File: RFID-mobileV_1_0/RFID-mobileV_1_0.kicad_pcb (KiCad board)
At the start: 2 copper layers, 52.9 x 145.1 mm, 53 parts, among them J1 USB_C_Receptacle_USB2.0, J2 Conn_01x05_Male, J3 Conn_01x05_Female, J4 Conn_01x05_Male, Q1 MMBT3904, SW1 SW_Push, U1 XC6206P332MR, U2 E22-400T22S, U3 STM32G030FxP, U4 LM321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

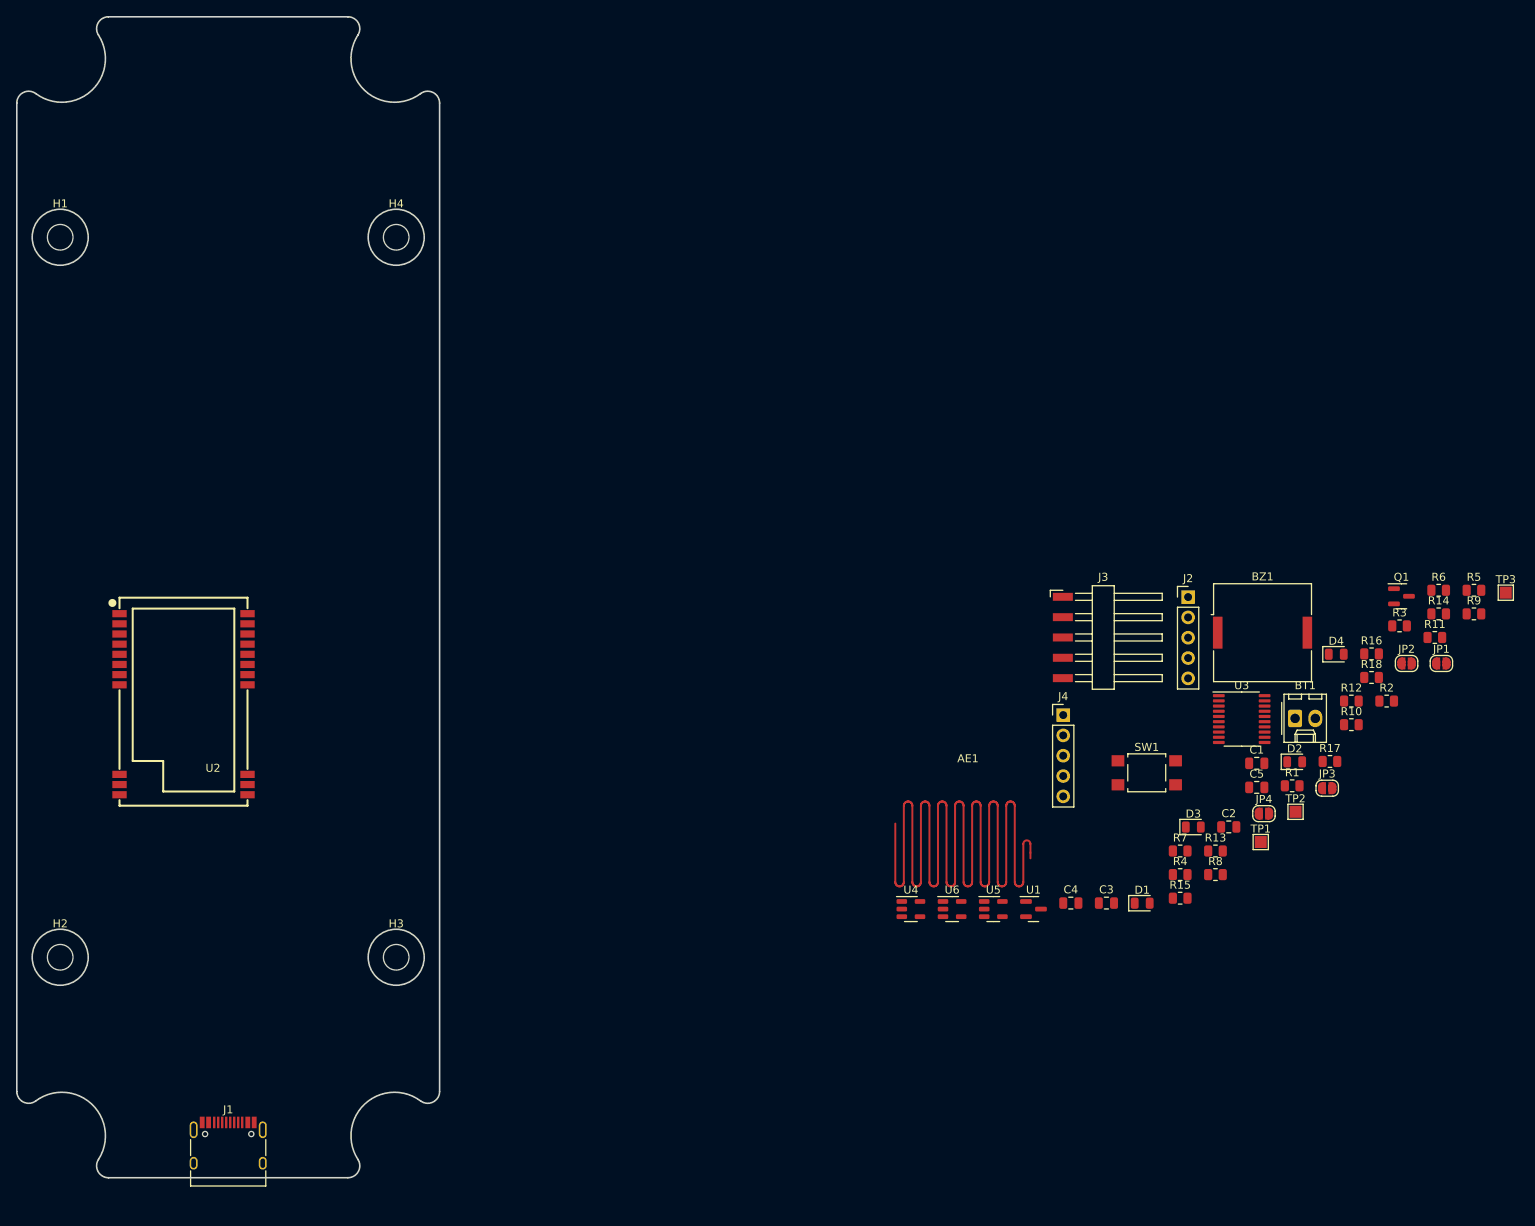
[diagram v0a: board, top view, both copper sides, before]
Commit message: Update RFID-mobileV_1_0.kicad_pcb
remove Case box
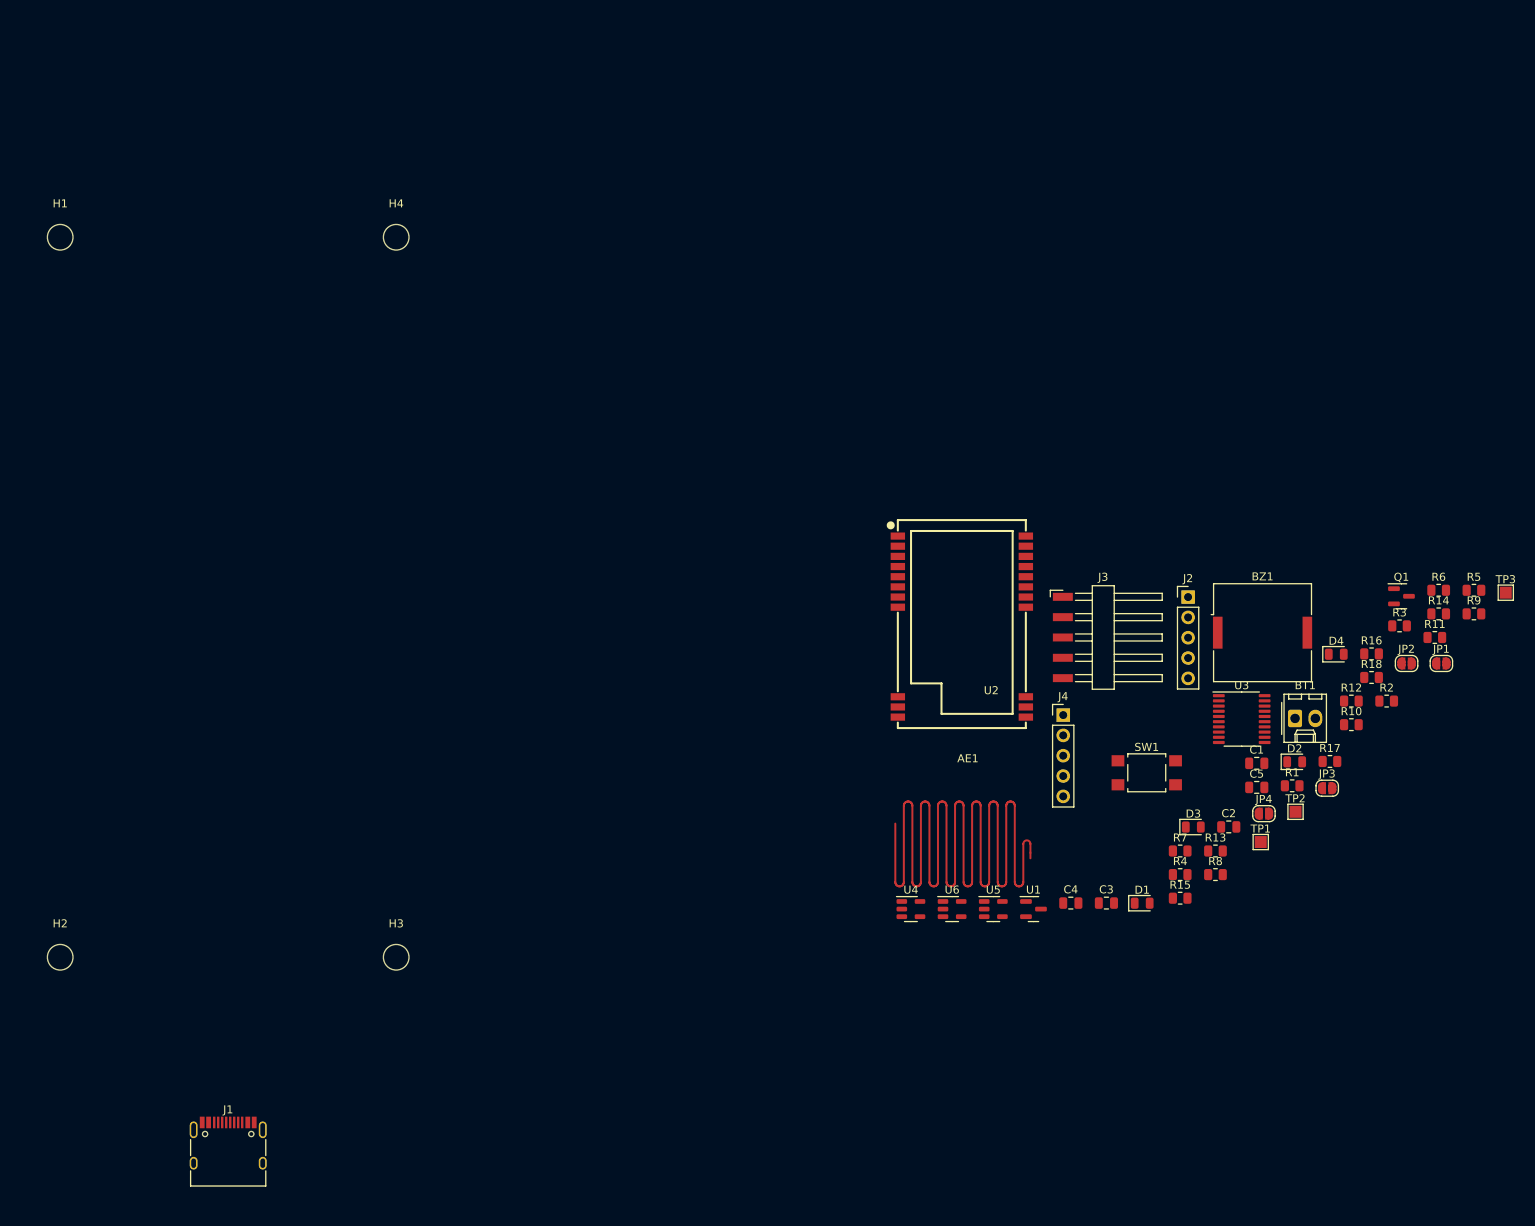
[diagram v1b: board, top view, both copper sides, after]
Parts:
- moved U2 97.8 mm to (179.8, 99.3)
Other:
- board outline removed
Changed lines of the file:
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@@
   )
   (footprint "RF_Module:E220-400TxxS" (layer "F.Cu")
-    (at 82.541 109.015)
+    (at 179.832 99.314)
     (property "LCSC" "C2903765")
     (property "Sheetfile" "RFID-mobileV_1_0.kicad_sch")
@@
       ))
   )
-  (gr_line (start 72.908528 168.471048) (end 102.836307 168.471048) (layer "Edge.Cuts") (width 0.2))
-  (gr_arc (start 61.44717 34.143343) (mid 62.267129 32.815576) (end 63.821508 32.954099) (layer "Edge.Cuts") (width 0.2))
-  (gr_circle (center 66.872419 140.913536) (end 70.372419 140.913536) (layer "Edge.Cuts") (width 0.2) (fill none))
-  (gr_arc (start 71.660076 25.645136) (mid 70.795729 32.575919) (end 63.821508 32.954099) (layer "Edge.Cuts") (width 0.2))
-  (gr_arc (start 71.660076 25.645136) (mid 71.604805 24.129998) (end 72.908528 23.356027) (layer "Edge.Cuts") (width 0.2))
-  (gr_arc (start 111.923327 32.954099) (mid 104.949099 32.575918) (end 104.084759 25.645136) (layer "Edge.Cuts") (width 0.2))
-  (gr_arc (start 102.836307 23.356027) (mid 104.14 24.13) (end 104.084759 25.645136) (layer "Edge.Cuts") (width 0.2))
-  (gr_arc (start 63.821508 158.872976) (mid 62.267129 159.011492) (end 61.44717 157.683732) (layer "Edge.Cuts") (width 0.2))
-  (gr_arc (start 63.821508 158.872976) (mid 70.795725 159.251162) (end 71.660076 166.181939) (layer "Edge.Cuts") (width 0.2))
-  (gr_arc (start 104.084759 166.181939) (mid 104.139996 167.697052) (end 102.836307 168.471048) (layer "Edge.Cuts") (width 0.2))
-  (gr_line (start 72.908528 23.356027) (end 102.836307 23.356027) (layer "Edge.Cuts") (width 0.2))
-  (gr_circle (center 66.872419 50.913536) (end 70.372419 50.913536) (layer "Edge.Cuts") (width 0.2) (fill none))
-  (gr_arc (start 72.908528 168.471048) (mid 71.604812 167.697077) (end 71.660076 166.181939) (layer "Edge.Cuts") (width 0.2))
-  (gr_arc (start 111.923327 32.954099) (mid 113.477726 32.815559) (end 114.297665 34.143343) (layer "Edge.Cuts") (width 0.2))
-  (gr_line (start 114.297665 34.143343) (end 114.297665 157.683732) (layer "Edge.Cuts") (width 0.2))
-  (gr_circle (center 108.872417 50.91354) (end 112.372417 50.91354) (layer "Edge.Cuts") (width 0.2) (fill none))
-  (gr_circle (center 108.872417 140.91354) (end 112.372417 140.91354) (layer "Edge.Cuts") (width 0.2) (fill none))
-  (gr_line (start 61.44717 157.683732) (end 61.44717 34.143343) (layer "Edge.Cuts") (width 0.2))
-  (gr_arc (start 114.297665 157.683732) (mid 113.477708 159.011459) (end 111.923327 158.872976) (layer "Edge.Cuts") (width 0.2))
-  (gr_arc (start 104.084759 166.181939) (mid 104.949088 159.251147) (end 111.923327 158.872976) (layer "Edge.Cuts") (width 0.2))
-  (group "" (id 41ef6d8e-078c-46e5-a743-15f86f94b1c5)
-    (members
-      0667208e-872f-444a-9ed0-78a1b5f392d2
-      0d1c133a-5b0b-4fe0-b915-2f72b13b37e9
-      22fd57c4-481e-4417-b920-694451210da2
-      24d3ee68-60f0-4c8a-a72b-065f1026fd87
-      31e2d26e-842a-4694-a3ae-7642d792727c
-      34d3baf1-c1a6-463d-a7da-03fde565ea93
-      3f1d3b22-3ba1-4783-af8d-526bce7c36db
-      449cc181-df4b-4d3b-93ef-0653c2171fe8
-      513c5122-3fbb-44b6-aa2c-74224719f915
-      524dc8d0-13b4-43fe-b274-8ac08bc4b894
-      7aad0cca-fb50-4041-9a10-5380cb0860ac
-      7fd11519-eb9e-4413-8ca2-e43e38c699f6
-      969d876f-dc87-40bf-9e96-03cbb9ea5e82
-      99162744-5eac-427e-9957-877587056aee
-      a8470270-920a-4fed-9691-22526135f92c
-      bc29a09d-ebbe-4bab-9edb-114e75ee17a4
-      da151d0a-a1fa-4865-aa78-eb4b6082fbfd
-      ec7073f7-f754-4ee6-a977-3d11d16480f8
-      eec347af-8fb3-4b2d-8e93-6e7176516f57
-      f99552ce-0729-4ada-aef3-5686270d7c4d
-    )
-  )
 )

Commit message: add
PCB Broad edge
place Device
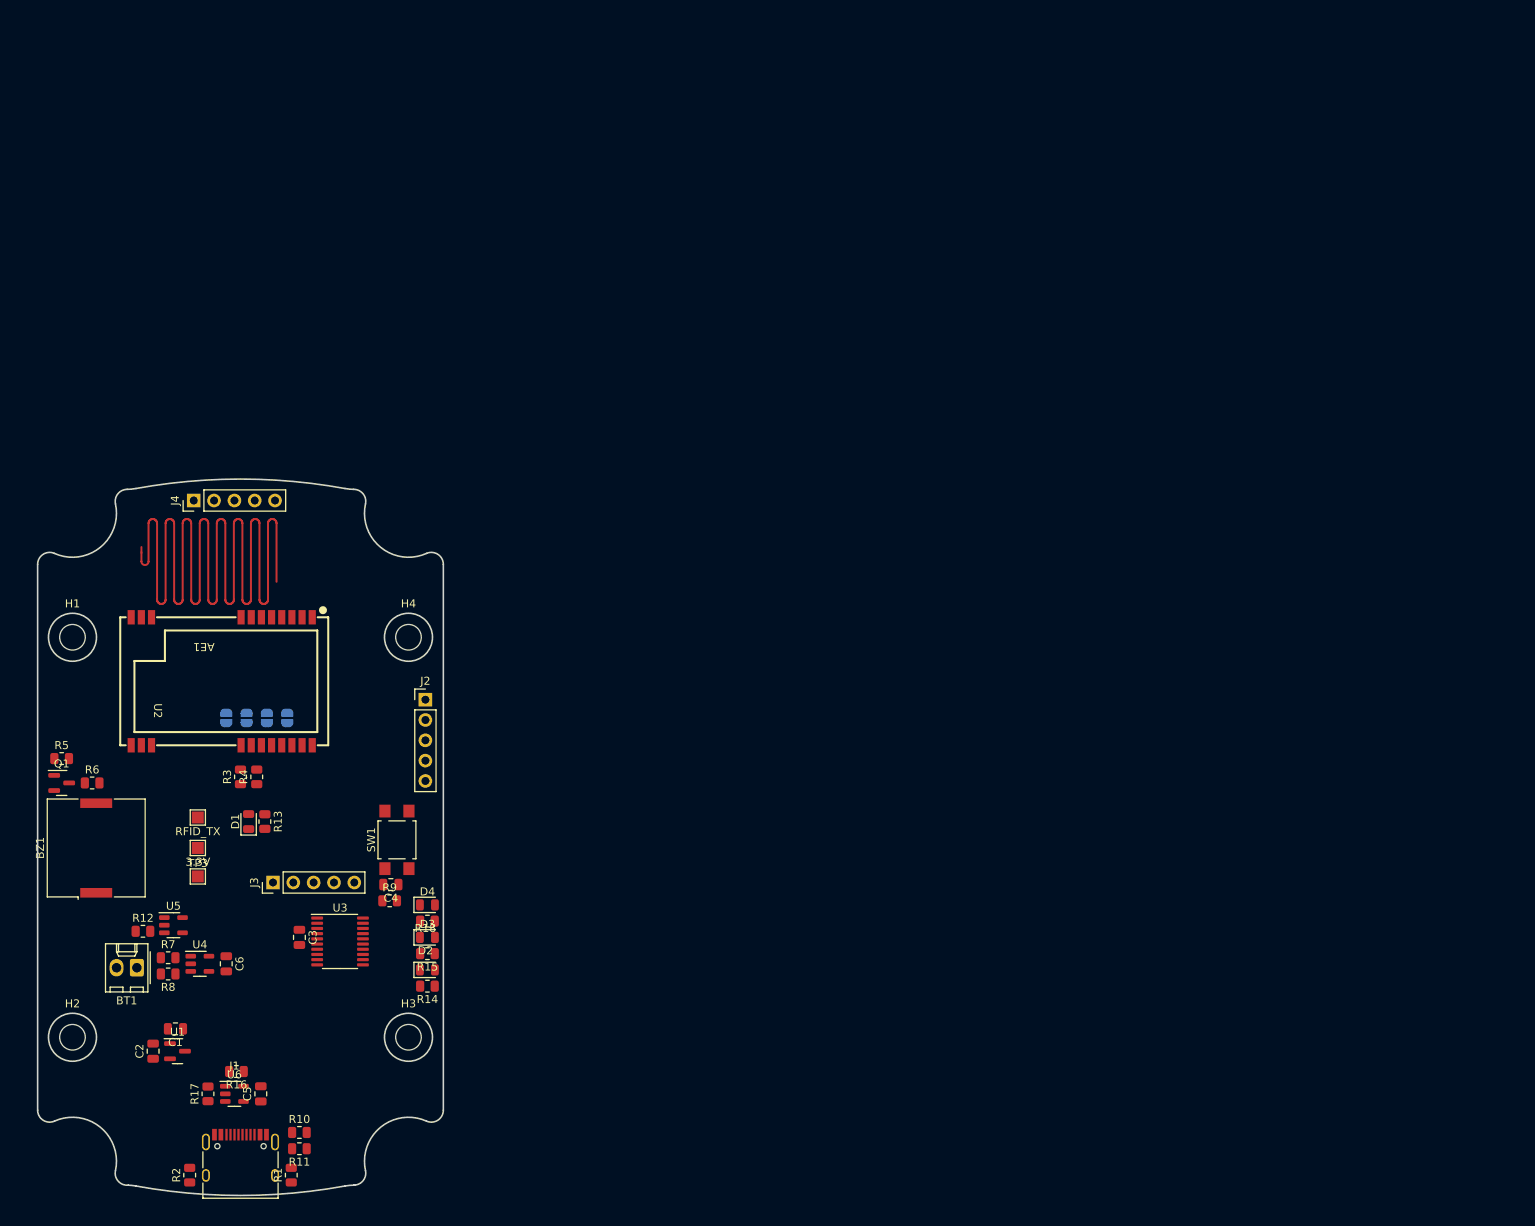
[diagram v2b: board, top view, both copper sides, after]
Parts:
- added C6: 0.1uF, Capacitor_SMD:C_0805_2012Metric, F.Cu at (87.6, 141.7)
- J3: footprint Connector_Harwin:Harwin_M20-89005xx_1x05_P2.54mm_Horizontal -> Connector_PinHeader_2.54mm:PinHeader_1x05_P2.54mm_Vertical
- JP1, JP2, JP3, JP4: moved to B.Cu
- TP1: value TestPoint -> RFID_TX
- TP2: value TestPoint -> 3.3V
- TP3: value TestPoint -> GND
- moved R5 177.8 mm to (67.1, 116.1)
- moved R6 170.0 mm to (70.9, 119.1)
- moved Q1 169.1 mm to (67.1, 119.1)
- moved TP3 167.3 mm to (84.1, 130.8)
- moved R2 160.9 mm to (83.1, 168.1), turned to 90 degrees
- moved R11 155.7 mm to (96.8, 164.8), turned to 180 degrees
- moved R12 153.8 mm to (77.2, 137.7)
- moved JP1 152.0 mm to (87.6, 111.0), turned to 90 degrees
- moved R16 151.2 mm to (88.9, 155.2), turned to 180 degrees
- moved BZ1 148.3 mm to (71.4, 127.3), turned to 90 degrees
- moved BT1 148.1 mm to (76.5, 142.2), turned to 180 degrees
- moved R17 146.3 mm to (85.3, 158.0), turned to 90 degrees
- moved R3 146.1 mm to (89.4, 118.4), turned to 90 degrees
- moved JP2 145.2 mm to (90.2, 111.0), turned to 90 degrees
- moved R10 141.0 mm to (96.8, 162.8)
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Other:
- board outline added: 50.7 x 89.5 mm

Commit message: update
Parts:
- moved TP2 27.7 mm to (109.0, 115.1)
- moved TP3 27.7 mm to (109.0, 118.6)
- moved TP1 27.6 mm to (109.0, 111.5)
- moved JP1 4.83 mm to (87.6, 106.2)
- moved JP2 4.83 mm to (90.2, 106.2)
- moved JP3 4.83 mm to (92.7, 106.2)
- moved JP4 4.83 mm to (95.2, 106.2)
- moved D2 3.71 mm to (113.5, 146.1), turned to 90 degrees
- moved R12 3.45 mm to (80.4, 139.0)
- moved D3 2.90 mm to (113.5, 141.2), turned to 90 degrees
- moved D4 2.17 mm to (113.5, 136.4), turned to 90 degrees
- moved R18 1.98 mm to (111.5, 134.9), turned to -90 degrees
- moved R15 1.48 mm to (111.5, 139.7), turned to -90 degrees
- moved R14 1.27 mm to (111.5, 144.6), turned to -90 degrees
- moved U5 0.79 mm to (80.7, 136.2)
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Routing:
- net /LoRa_RXD: track 0.00 -> 58.6 mm, vias 0 -> 1
- net /LoRa_TXD: track 0.00 -> 55.5 mm, vias 0 -> 1
- net /LoRa_AUX: track 0.00 -> 51.8 mm
- net /NRST: track 0.00 -> 34.9 mm, vias 0 -> 2
- net /LoRa_RXD_: track 0.00 -> 28.8 mm, vias 0 -> 1
- net /LoRa_TXD_: track 0.00 -> 25.3 mm, vias 0 -> 1
- net +3V3: track 0.00 -> 20.7 mm
- net /PA6: track 0.00 -> 13.1 mm
- net /ANT: track 0.00 -> 12.2 mm
- net /SWDIO: track 0.00 -> 10.3 mm
- net /PA7: track 0.00 -> 9.93 mm, vias 0 -> 2
- net /PA8: track 0.00 -> 9.62 mm, vias 0 -> 2
- net /M0: track 0.00 -> 8.89 mm, vias 0 -> 1
- net /M1: track 0.00 -> 8.36 mm, vias 0 -> 1
- net /SWCLK: track 0.00 -> 7.52 mm
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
